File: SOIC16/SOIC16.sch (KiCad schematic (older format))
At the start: 3 parts, among them J1 Conn_02x08_Counter_Clockwise, J2 Conn_01x08, J3 Conn_01x08

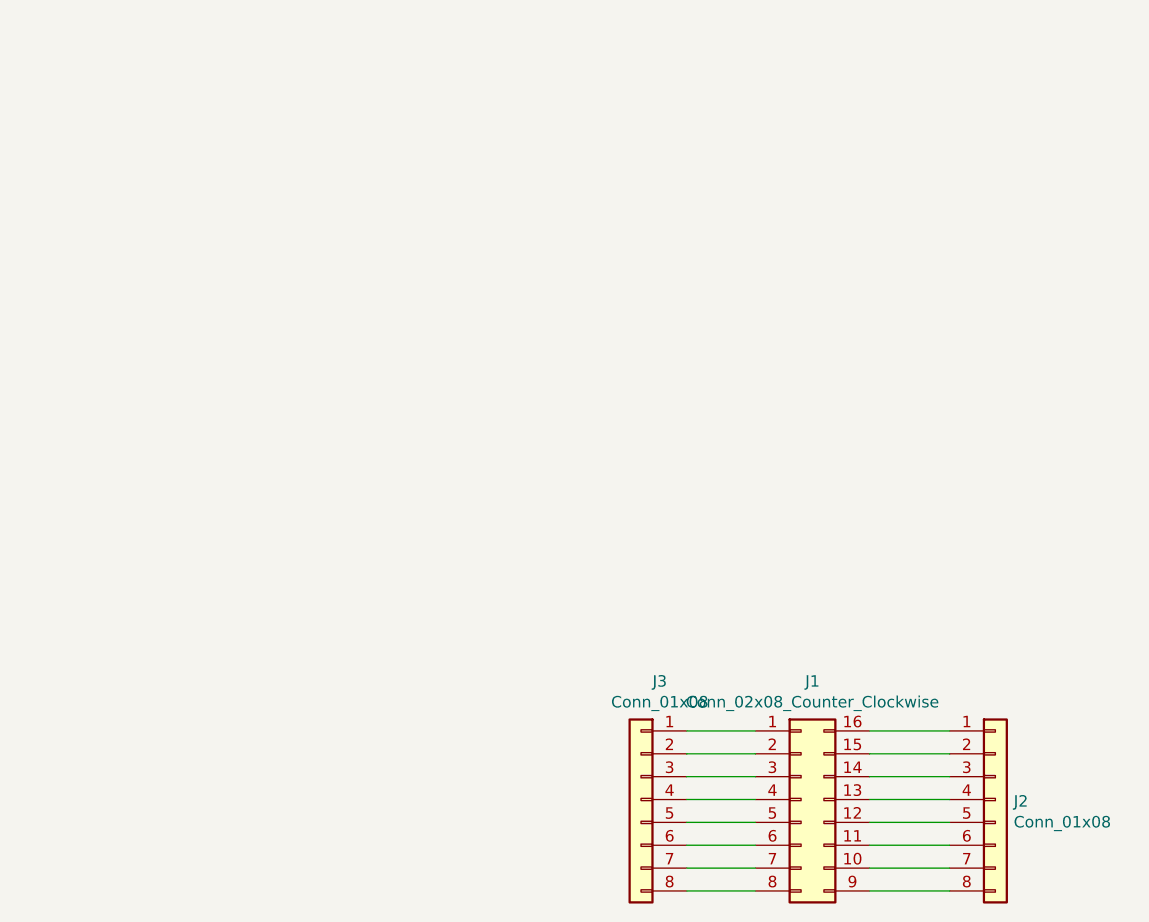
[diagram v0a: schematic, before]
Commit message: USB, SD and CR Cells Added
MicroSD, MicroUSB, MiniUSB, USB-C, CR1220, CR2032 added as well as all schematics page sizes optimised
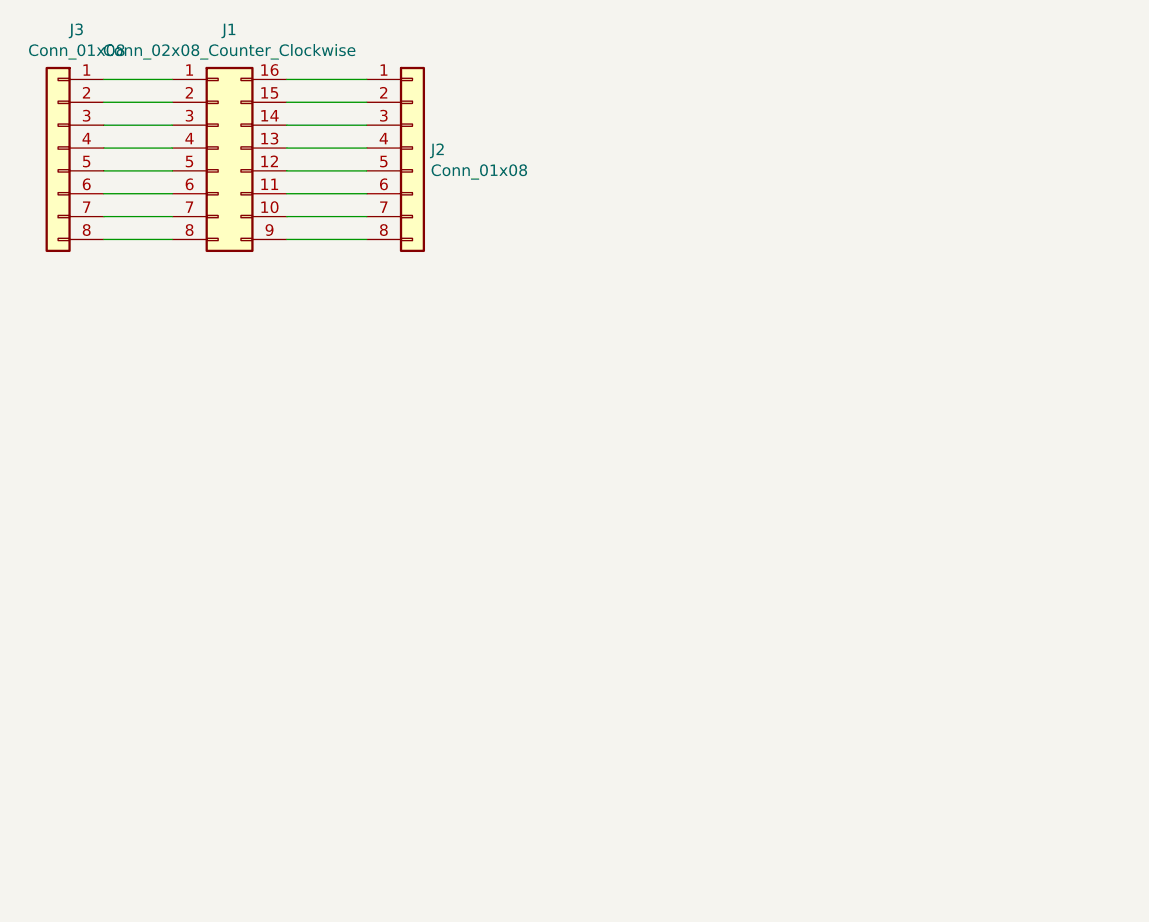
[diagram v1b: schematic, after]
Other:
- moved on the sheet: J1, J2, J3
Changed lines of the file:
@@
 EESchema Schematic File Version 4
-LIBS:SOIC28-cache
+LIBS:SOIC16-cache
 EELAYER 29 0
 EELAYER END
-$Descr A4 11693 8268
+$Descr User 5197 4016
 encoding utf-8
 Sheet 1 1
-Title ""
-Date ""
-Rev ""
-Comp ""
-Comment1 ""
-Comment2 ""
-Comment3 ""
+Title "SOIC16 To DIP16 Breakout Board"
+Date "2019-07-04"
+Rev "1"
+Comp "SirBoard"
+Comment1 "SOIC16 P = 1.27mm"
+Comment2 "TSSOP P = 0.65mm"
+Comment3 "DIP P = 2.54mm"
 Comment4 ""
 $EndDescr
@@
 L Connector_Generic:Conn_01x08 J2
 U 1 1 5D1CFB0A
-P 5950 4200
-F 0 "J2" H 6030 4192 50  0000 L CNN
-F 1 "Conn_01x08" H 6030 4101 50  0000 L CNN
-F 2 "Connector_PinHeader_2.54mm:PinHeader_1x08_P2.54mm_Vertical" H 5950 4200 50  0001 C CNN
-F 3 "~" H 5950 4200 50  0001 C CNN
-	1    5950 4200
+P 3400 1350
+F 0 "J2" H 3480 1342 50  0000 L CNN
+F 1 "Conn_01x08" H 3480 1251 50  0000 L CNN
+F 2 "Connector_PinHeader_2.54mm:PinHeader_1x08_P2.54mm_Vertical" H 3400 1350 50  0001 C CNN
+F 3 "~" H 3400 1350 50  0001 C CNN
+	1    3400 1350
 	1    0    0    -1
 $EndComp
@@
 L Connector_Generic:Conn_01x08 J3
 U 1 1 5D1CFF0A
-P 4400 4200
-F 0 "J3" H 4318 4717 50  0000 C CNN
-F 1 "Conn_01x08" H 4318 4626 50  0000 C CNN
-F 2 "Connector_PinHeader_2.54mm:PinHeader_1x08_P2.54mm_Vertical" H 4400 4200 50  0001 C CNN
-F 3 "~" H 4400 4200 50  0001 C CNN
-	1    4400 4200
+P 1850 1350
+F 0 "J3" H 1768 1867 50  0000 C CNN
+F 1 "Conn_01x08" H 1768 1776 50  0000 C CNN
+F 2 "Connector_PinHeader_2.54mm:PinHeader_1x08_P2.54mm_Vertical" H 1850 1350 50  0001 C CNN
+F 3 "~" H 1850 1350 50  0001 C CNN
+	1    1850 1350
 	-1   0    0    -1
 $EndComp
@@
 L Connector_Generic:Conn_02x08_Counter_Clockwise J1
 U 1 1 5D1DAB32
-P 5100 4200
-F 0 "J1" H 5150 4717 50  0000 C CNN
-F 1 "Conn_02x08_Counter_Clockwise" H 5150 4626 50  0000 C CNN
-F 2 "Package_SO:SOIC-16_3.9x9.9mm_P1.27mm" H 5100 4200 50  0001 C CNN
-F 3 "~" H 5100 4200 50  0001 C CNN
-	1    5100 4200
+P 2550 1350
+F 0 "J1" H 2600 1867 50  0000 C CNN
+F 1 "Conn_02x08_Counter_Clockwise" H 2600 1776 50  0000 C CNN
+F 2 "Package_SO:SOIC-16_3.9x9.9mm_P1.27mm" H 2550 1350 50  0001 C CNN
+F 3 "~" H 2550 1350 50  0001 C CNN
+	1    2550 1350
 	1    0    0    -1
 $EndComp
 Wire Wire Line
-	4600 3900 4900 3900
+	2050 1050 2350 1050
 Wire Wire Line
-	4900 4000 4600 4000
+	2350 1150 2050 1150
 Wire Wire Line
-	4600 4100 4900 4100
+	2050 1250 2350 1250
 Wire Wire Line
-	4900 4200 4600 4200
+	2350 1350 2050 1350
 Wire Wire Line
-	4600 4300 4900 4300
+	2050 1450 2350 1450
 Wire Wire Line
-	4900 4400 4600 4400
+	2350 1550 2050 1550
 Wire Wire Line
-	4600 4500 4900 4500
+	2050 1650 2350 1650
 Wire Wire Line
-	4900 4600 4600 4600
+	2350 1750 2050 1750
 Wire Wire Line
-	5400 3900 5750 3900
+	2850 1050 3200 1050
 Wire Wire Line
-	5750 4000 5400 4000
+	3200 1150 2850 1150
 Wire Wire Line
-	5400 4100 5750 4100
+	2850 1250 3200 1250
 Wire Wire Line
-	5750 4200 5400 4200
+	3200 1350 2850 1350
 Wire Wire Line
-	5400 4300 5750 4300
+	2850 1450 3200 1450
 Wire Wire Line
-	5750 4400 5400 4400
+	3200 1550 2850 1550
 Wire Wire Line
-	5400 4500 5750 4500
+	2850 1650 3200 1650
 Wire Wire Line
-	5750 4600 5400 4600
+	3200 1750 2850 1750
 $EndSCHEMATC
